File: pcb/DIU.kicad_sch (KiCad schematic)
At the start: 62 parts, among them J1 Conn_01x02_Pin, J18 Battery, J2 Conn_01x02_Pin, J3 Conn_01x03_Pin, J4 USB_OTG, J5 Conn_01x03_Socket, Q1 2N7002E, SW1 SW_SPST, SW2 SW_SPST, SW3 SW_SPST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

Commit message: Partlist refactoring
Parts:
- BZ1: Hersteller DigiKey -> (none); Nummer 668-1468-ND -> (none); Vendor (none) -> HTL; VendorId (none) -> 102851
- C1, C32: Hersteller HTL -> (none); Nummer 103250 -> (none); Vendor (none) -> HTL; VendorId (none) -> 103250
- C2: Hersteller HTL -> (none); Nummer 100139 -> (none); Vendor (none) -> HTL; VendorId (none) -> 100139
- C3: Hersteller HTL -> (none); Nummer 100140 -> (none); Vendor (none) -> HTL; VendorId (none) -> 100140
- C30, C31: Hersteller HTL -> (none); Nummer 103323 -> (none); Vendor (none) -> HTL; VendorId (none) -> 103323
- C4, C6: Hersteller HTL -> (none); Nummer 102856 -> (none); Vendor (none) -> HTL; VendorId (none) -> 102856
- C5, C7: Hersteller HTL -> (none); Nummer 100128 -> (none); Vendor (none) -> HTL; VendorId (none) -> 100128
- D89, D90: Hersteller DigiKey -> (none); Nummer 160-1830-1-ND, 160-1828-1-ND, 4 x 160-1827-1-ND -> (none); Vendor (none) -> HTL; VendorId (none) -> 103438, 103439, 4 x 103440
- D91: Hersteller HTL -> (none); Nummer 103254 -> (none); Vendor (none) -> HTL; VendorId (none) -> 103254
- F1: Hersteller DigiKey -> (none); Nummer 507-1803-1-ND -> (none); Vendor (none) -> HTL; VendorId (none) -> 101639
- H1, H2: Hersteller HTL -> (none); Nummer 101034, 101382 -> (none); Vendor (none) -> HTL; VendorId (none) -> 101034, 101382
- H3, H4: Hersteller HTL -> (none); Nummer 101017 -> (none); Vendor (none) -> HTL; VendorId (none) -> 101017
- J1, J2, J3: Hersteller HTL -> (none); Nummer 101521 -> (none); Vendor (none) -> HTL; VendorId (none) -> 101521
- J18: Hersteller DigiKey -> (none); Nummer BAT-HLD-012-SMT-ND -> (none); Vendor (none) -> HTL; VendorId (none) -> 103442
- J4: Hersteller HTL -> (none); Nummer 103441 -> (none); Vendor (none) -> HTL; VendorId (none) -> 103441
- Q1: Hersteller DigiKey -> (none); Nummer 4530-2N7002ECT-ND -> (none); Vendor (none) -> HTL; VendorId (none) -> 103443
- R100, R99: Hersteller HTL -> (none); Nummer 103202 -> (none); Vendor (none) -> HTL; VendorId (none) -> 103202
- R89, R90: Hersteller HTL -> (none); Nummer 103178 -> (none); Vendor (none) -> HTL; VendorId (none) -> 103178
- R91, R94: Hersteller HTL -> (none); Nummer 103141 -> (none); Vendor (none) -> HTL; VendorId (none) -> 103141
- R92, R93: Hersteller HTL -> (none); Nummer 103164 -> (none); Vendor (none) -> HTL; VendorId (none) -> 103164
- R95: Hersteller HTL -> (none); Nummer 103194 -> (none); Vendor (none) -> HTL
- R96: Hersteller HTL -> (none); Nummer 103202 -> (none); Vendor (none) -> HTL
- R97, R98: Hersteller HTL -> (none); Nummer 102951 -> (none); Vendor (none) -> HTL; VendorId (none) -> 102951
- SW1, SW2, SW3, SW4: Hersteller DigiKey -> (none); Nummer PTS647SM70SMTR2LFSCT-ND -> (none); Vendor (none) -> HTL; VendorId (none) -> 101614
- U1: Hersteller DigiKey -> (none); Nummer 497-3455-1-ND -> (none); Vendor (none) -> HTL; VendorId (none) -> 103444
- U15: Hersteller DigiKey -> (none); Nummer MCP7940NT-I/SNCT-ND -> (none); Vendor (none) -> HTL; VendorId (none) -> 103446
- U2: Hersteller RS -> (none); Nummer 406-580 -> (none); Vendor (none) -> HTL; VendorId (none) -> 103271
- U3: Hersteller DigiKey -> (none); Nummer ATTINY1606-SN-ND -> (none); Vendor (none) -> HTL; VendorId (none) -> 103450
- Y1: Hersteller DigiKey -> (none); Nummer 644-MU00525-32.768KCT-ND -> (none); Vendor (none) -> HTL; VendorId (none) -> 103447

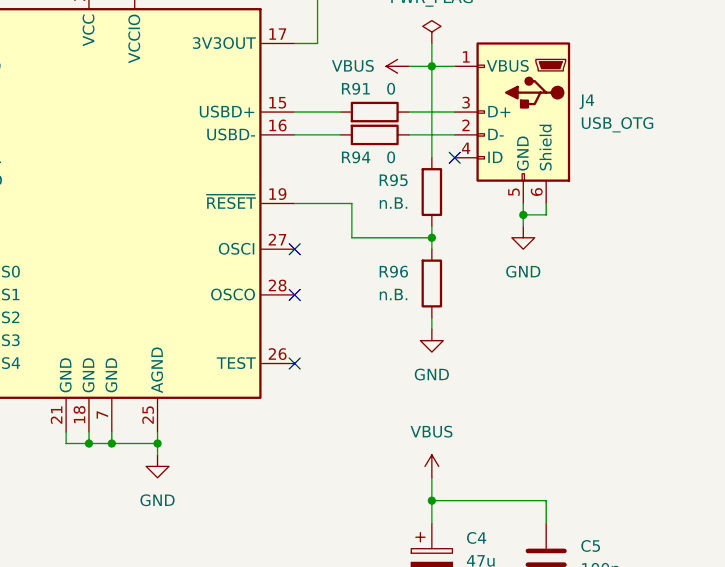
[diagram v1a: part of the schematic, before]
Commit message: Change reset circuit
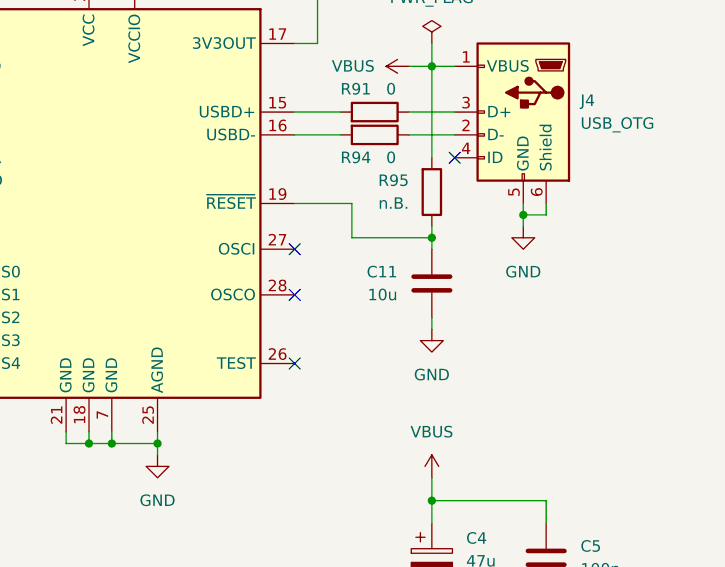
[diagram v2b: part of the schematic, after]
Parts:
- removed R96: n.B., Resistor_SMD:R_0603_1608Metric, symbol Device:R
- added C11: 10u, Capacitor_SMD:C_0603_1608Metric, symbol Device:C
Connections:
- net GND: now also C11.1
- net at R95.1, U2.19 (~{RESET}): now also C11.2
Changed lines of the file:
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@@
+    )
+  )
+  (symbol (lib_id "Device:C") (at 250.19 64.77 0) (mirror x) (unit 1)
+    (in_bom yes) (on_board yes) (dnp no) (fields_autoplaced)
+    (property "Reference" "C11" (at 246.38 63.5 0)
+      (effects (font (size 1.27 1.27)) (justify right))
+    )
+    (property "Value" "10u" (at 246.38 66.04 0)
+      (effects (font (size 1.27 1.27)) (justify right))
+    )
+    (property "Footprint" "Capacitor_SMD:C_0603_1608Metric" (at 251.1552 60.96 0)
+      (effects (font (size 1.27 1.27)) hide)
+    )
+    (property "Datasheet" "~" (at 250.19 64.77 0)
+      (effects (font (size 1.27 1.27)) hide)
+    )
+    (property "Vendor" "HTL" (at 250.19 64.77 0)
+      (effects (font (size 1.27 1.27)) hide)
+    )
+    (property "VendorId" "100137" (at 250.19 64.77 0)
+      (effects (font (size 1.27 1.27)) hide)
+    )
+    (pin "1")
+    (pin "2")
+    (instances
+      (project "DIU"
+        (path "/aa6ef36a-0508-4748-be9d-33919bd2eaaf"
+          (reference "C11") (unit 1)
+        )
+      )
     )
   )
@@
         )
       )
-    )
-  )
-  (symbol (lib_id "Device:R") (at 250.19 64.77 0) (mirror x) (unit 1)
-    (in_bom yes) (on_board yes) (dnp no) (fields_autoplaced)
-    (property "Reference" "R96" (at 247.65 63.5 0)
-      (effects (font (size 1.27 1.27)) (justify right))
-    )
-    (property "Value" "n.B." (at 247.65 66.04 0)
-      (effects (font (size 1.27 1.27)) (justify right))
-    )
-    (property "Footprint" "Resistor_SMD:R_0603_1608Metric" (at 248.412 64.77 90)
-      (effects (font (size 1.27 1.27)) hide)
-    )
-    (property "Datasheet" "~" (at 250.19 64.77 0)
-      (effects (font (size 1.27 1.27)) hide)
-    )
-    (property "Vendor" "HTL" (at 250.19 64.77 0)
-      (effects (font (size 1.27 1.27)) hide)
-    )
-    (property "VendorId" "" (at 250.19 64.77 0)
-      (effects (font (size 1.27 1.27)) hide)
-    )
-    (pin "2")
-    (pin "1")
-    (instances
-      (project "DIU"
-        (path "/aa6ef36a-0508-4748-be9d-33919bd2eaaf"
-          (reference "R96") (unit 1)
-        )
-      )

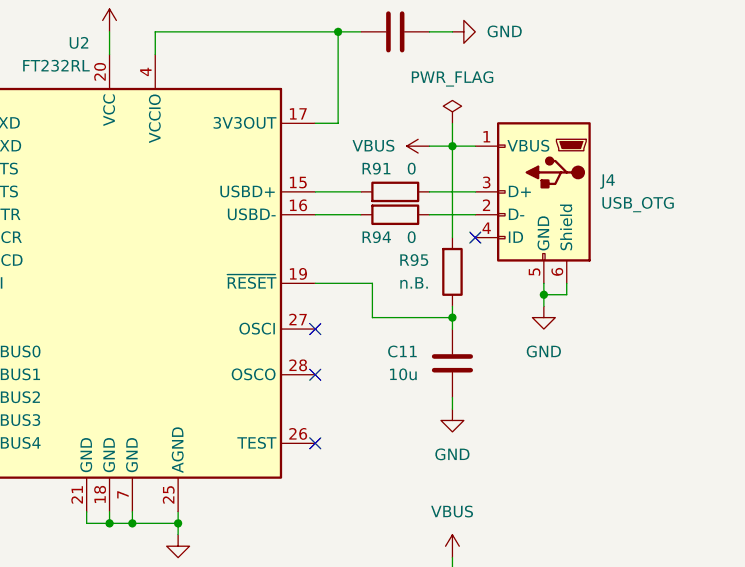
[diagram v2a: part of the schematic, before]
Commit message: Add resistor to reset circuit
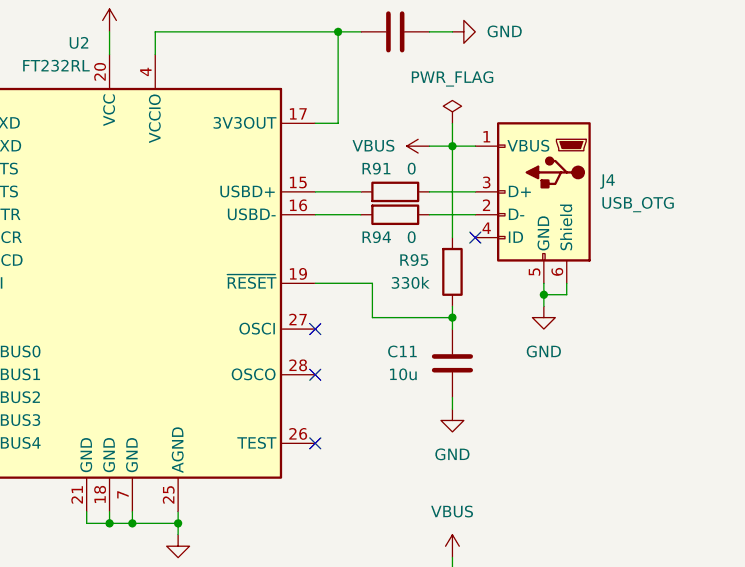
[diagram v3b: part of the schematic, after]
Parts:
- R95: value n.B. -> 330k; VendorId (none) -> 103238
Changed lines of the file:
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@@
       (effects (font (size 1.27 1.27)) (justify right))
     )
-    (property "Value" "n.B." (at 247.65 55.88 0)
+    (property "Value" "330k" (at 247.65 55.88 0)
       (effects (font (size 1.27 1.27)) (justify right))
     )
@@
       (effects (font (size 1.27 1.27)) hide)
     )
-    (property "VendorId" "" (at 250.19 54.61 0)
+    (property "VendorId" "103238" (at 250.19 54.61 0)
       (effects (font (size 1.27 1.27)) hide)
     )

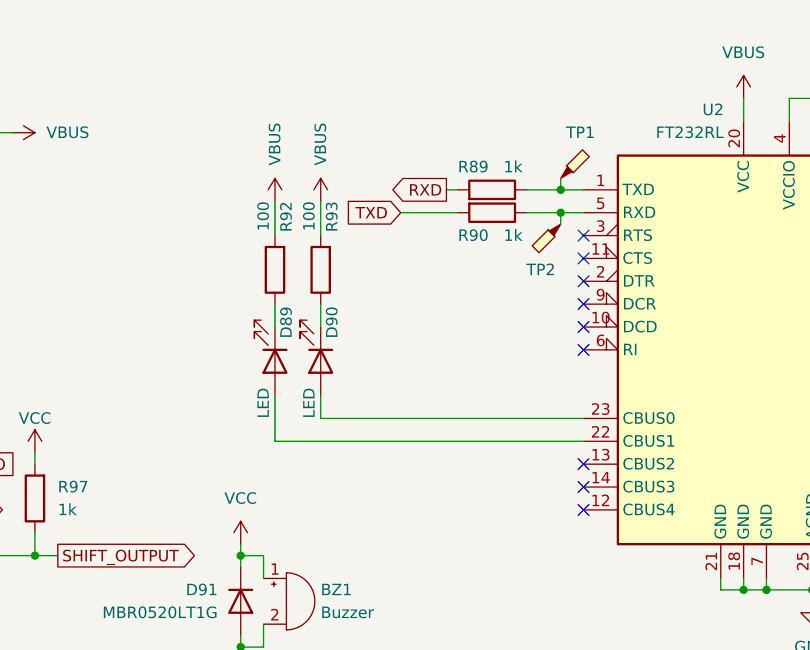
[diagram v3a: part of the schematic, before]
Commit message: Fix wrong led polarity
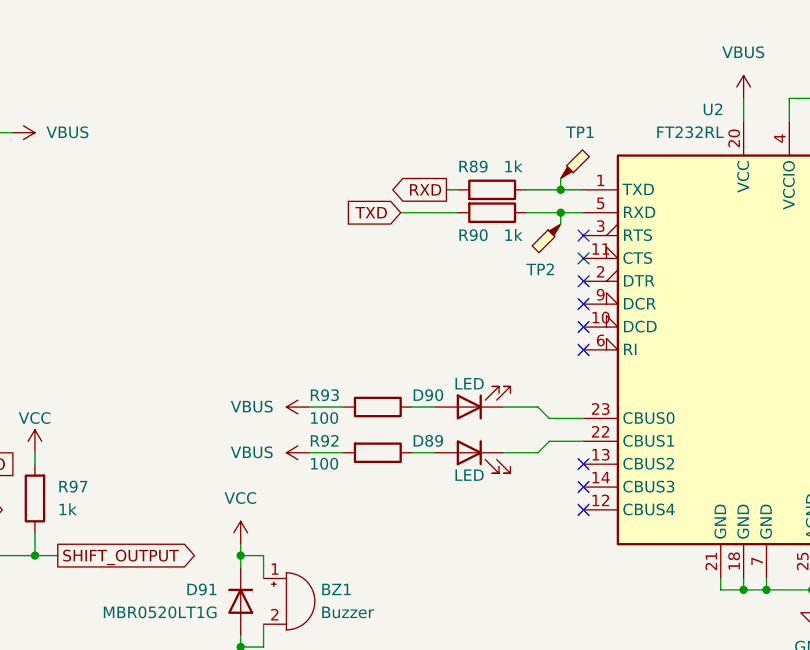
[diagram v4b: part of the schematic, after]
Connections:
- net at U2.22 (CBUS1): now also D89.1 (K); no longer D89.2 (A)
- net at U2.23 (CBUS0): now also D90.1 (K); no longer D90.2 (A)
- net at R92.1: now also D89.2 (A); no longer D89.1 (K)
- net at R93.1: now also D90.2 (A); no longer D90.1 (K)
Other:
- moved on the sheet: D89, D90, R92, R93
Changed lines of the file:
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@@
     (stroke (width 0) (type default))
   )
-  (wire (pts (xy 165.1 53.34) (xy 165.1 50.8))
+  (wire (pts (xy 177.8 62.23) (xy 175.26 62.23))
     (stroke (width 0) (type default))
   )
@@
     (stroke (width 0) (type default))
   )
-  (wire (pts (xy 165.1 43.18) (xy 165.1 39.37))
+  (wire (pts (xy 167.64 62.23) (xy 163.83 62.23))
     (stroke (width 0) (type default))
   )
@@
     (stroke (width 0) (type default))
   )
+  (wire (pts (xy 185.42 62.23) (xy 189.23 62.23))
+    (stroke (width 0) (type default))
+  )
   (wire (pts (xy 190.5 127) (xy 190.5 129.54))
     (stroke (width 0) (type default))
@@
     (stroke (width 0) (type default))
   )
+  (wire (pts (xy 190.5 66.04) (xy 194.31 66.04))
+    (stroke (width 0) (type default))
+  )
   (wire (pts (xy 76.2 40.64) (xy 76.2 43.18))
     (stroke (width 0) (type default))
@@
     (stroke (width 0) (type default))
   )
+  (wire (pts (xy 190.5 66.04) (xy 189.23 67.31))
+    (stroke (width 0) (type default))
+  )
   (wire (pts (xy 104.14 99.06) (xy 114.3 99.06))
     (stroke (width 0) (type default))
@@
     (stroke (width 0) (type default))
   )
-  (wire (pts (xy 160.02 66.04) (xy 160.02 60.96))
-    (stroke (width 0) (type default))
-  )
-  (wire (pts (xy 160.02 43.18) (xy 160.02 39.37))
+  (wire (pts (xy 167.64 67.31) (xy 163.83 67.31))
     (stroke (width 0) (type default))
   )
@@
     (stroke (width 0) (type default))
   )
-  (wire (pts (xy 72.39 30.48) (xy 76.2 30.48))
+  (wire (pts (xy 190.5 63.5) (xy 189.23 62.23))
     (stroke (width 0) (type default))
   )
-  (wire (pts (xy 194.31 66.04) (xy 160.02 66.04))
+  (wire (pts (xy 72.39 30.48) (xy 76.2 30.48))
     (stroke (width 0) (type default))
   )
@@
     (stroke (width 0) (type default))
   )
+  (wire (pts (xy 194.31 63.5) (xy 190.5 63.5))
+    (stroke (width 0) (type default))
+  )
   (wire (pts (xy 128.27 147.32) (xy 130.81 147.32))
     (stroke (width 0) (type default))
@@
     (stroke (width 0) (type default))
   )
-  (wire (pts (xy 165.1 60.96) (xy 165.1 63.5))
-    (stroke (width 0) (type default))
-  )
   (wire (pts (xy 53.34 88.9) (xy 53.34 96.52))
     (stroke (width 0) (type default))
@@
     (stroke (width 0) (type default))
   )
-  (wire (pts (xy 160.02 53.34) (xy 160.02 50.8))
+  (wire (pts (xy 177.8 67.31) (xy 175.26 67.31))
     (stroke (width 0) (type default))
   )
@@
     (stroke (width 0) (type default))
   )
-  (wire (pts (xy 194.31 63.5) (xy 165.1 63.5))
-    (stroke (width 0) (type default))
-  )
   (wire (pts (xy 250.19 58.42) (xy 250.19 59.69))
     (stroke (width 0) (type default))
@@
     (stroke (width 0) (type default))
   )
+  (wire (pts (xy 185.42 67.31) (xy 189.23 67.31))
+    (stroke (width 0) (type default))
+  )
   (wire (pts (xy 156.21 88.9) (xy 156.21 87.63))
     (stroke (width 0) (type default))
@@
     )
   )
-  (symbol (lib_id "power:VBUS") (at 160.02 39.37 0) (unit 1)
+  (symbol (lib_id "power:VBUS") (at 163.83 67.31 90) (unit 1)
     (in_bom yes) (on_board yes) (dnp no)
-    (property "Reference" "#PWR097" (at 160.02 43.18 0)
+    (property "Reference" "#PWR097" (at 167.64 67.31 0)
       (effects (font (size 1.27 1.27)) hide)
     )
-    (property "Value" "VBUS" (at 160.02 33.02 90)
+    (property "Value" "VBUS" (at 157.48 67.31 90)
       (effects (font (size 1.27 1.27)))
     )
-    (property "Footprint" "" (at 160.02 39.37 0)
+    (property "Footprint" "" (at 163.83 67.31 0)
       (effects (font (size 1.27 1.27)) hide)
     )
-    (property "Datasheet" "" (at 160.02 39.37 0)
+    (property "Datasheet" "" (at 163.83 67.31 0)
       (effects (font (size 1.27 1.27)) hide)
     )
@@
     )
   )
-  (symbol (lib_id "Device:R") (at 160.02 46.99 180) (unit 1)
+  (symbol (lib_id "Device:R") (at 171.45 67.31 270) (unit 1)
     (in_bom yes) (on_board yes) (dnp no)
-    (property "Reference" "R92" (at 161.29 39.37 90)
+    (property "Reference" "R92" (at 163.83 66.04 90)
       (effects (font (size 1.27 1.27)) (justify left))
     )
-    (property "Value" "100" (at 158.75 39.37 90)
+    (property "Value" "100" (at 163.83 68.58 90)
       (effects (font (size 1.27 1.27)) (justify left))
     )
-    (property "Footprint" "Resistor_SMD:R_0603_1608Metric" (at 161.798 46.99 90)
+    (property "Footprint" "Resistor_SMD:R_0603_1608Metric" (at 171.45 65.532 90)
       (effects (font (size 1.27 1.27)) hide)
     )
-    (property "Datasheet" "~" (at 160.02 46.99 0)
+    (property "Datasheet" "~" (at 171.45 67.31 0)
       (effects (font (size 1.27 1.27)) hide)
     )
-    (property "Vendor" "HTL" (at 160.02 46.99 0)
+    (property "Vendor" "HTL" (at 171.45 67.31 0)
       (effects (font (size 1.27 1.27)) hide)
     )
-    (property "VendorId" "103164" (at 160.02 46.99 0)
+    (property "VendorId" "103164" (at 171.45 67.31 0)
       (effects (font (size 1.27 1.27)) hide)
     )
@@
     )
   )
-  (symbol (lib_id "power:VBUS") (at 165.1 39.37 0) (unit 1)
+  (symbol (lib_id "power:VBUS") (at 163.83 62.23 90) (unit 1)
     (in_bom yes) (on_board yes) (dnp no)
-    (property "Reference" "#PWR098" (at 165.1 43.18 0)
+    (property "Reference" "#PWR098" (at 167.64 62.23 0)
       (effects (font (size 1.27 1.27)) hide)
     )
-    (property "Value" "VBUS" (at 165.1 33.02 90)
+    (property "Value" "VBUS" (at 157.48 62.23 90)
       (effects (font (size 1.27 1.27)))
     )
-    (property "Footprint" "" (at 165.1 39.37 0)
+    (property "Footprint" "" (at 163.83 62.23 0)
       (effects (font (size 1.27 1.27)) hide)
     )
-    (property "Datasheet" "" (at 165.1 39.37 0)
+    (property "Datasheet" "" (at 163.83 62.23 0)
       (effects (font (size 1.27 1.27)) hide)
     )
@@
     )
   )
-  (symbol (lib_id "Device:R") (at 165.1 46.99 180) (unit 1)
+  (symbol (lib_id "Device:R") (at 171.45 62.23 270) (unit 1)
     (in_bom yes) (on_board yes) (dnp no)
-    (property "Reference" "R93" (at 166.37 39.37 90)
+    (property "Reference" "R93" (at 163.83 60.96 90)
       (effects (font (size 1.27 1.27)) (justify left))
     )
-    (property "Value" "100" (at 163.83 39.37 90)
+    (property "Value" "100" (at 163.83 63.5 90)
       (effects (font (size 1.27 1.27)) (justify left))
     )
-    (property "Footprint" "Resistor_SMD:R_0603_1608Metric" (at 166.878 46.99 90)
+    (property "Footprint" "Resistor_SMD:R_0603_1608Metric" (at 171.45 60.452 90)
       (effects (font (size 1.27 1.27)) hide)
     )
-    (property "Datasheet" "~" (at 165.1 46.99 0)
+    (property "Datasheet" "~" (at 171.45 62.23 0)
       (effects (font (size 1.27 1.27)) hide)
     )
-    (property "Vendor" "HTL" (at 165.1 46.99 0)
+    (property "Vendor" "HTL" (at 171.45 62.23 0)
       (effects (font (size 1.27 1.27)) hide)
     )
-    (property "VendorId" "103164" (at 165.1 46.99 0)
+    (property "VendorId" "103164" (at 171.45 62.23 0)
       (effects (font (size 1.27 1.27)) hide)
     )
@@
     )
   )
-  (symbol (lib_id "Device:LED") (at 160.02 57.15 270) (unit 1)
+  (symbol (lib_id "Device:LED") (at 181.61 67.31 0) (mirror y) (unit 1)
     (in_bom yes) (on_board yes) (dnp no)
-    (property "Reference" "D89" (at 161.29 54.61 0)
+    (property "Reference" "D89" (at 175.26 66.04 0)
       (effects (font (size 1.27 1.27)) (justify right))
     )
-    (property "Value" "LED" (at 158.75 63.5 0)
-      (effects (font (size 1.27 1.27)) (justify right))
+    (property "Value" "LED" (at 181.61 69.85 0)
+      (effects (font (size 1.27 1.27)))
     )
-    (property "Footprint" "LED_SMD:LED_0603_1608Metric" (at 160.02 57.15 0)
+    (property "Footprint" "LED_SMD:LED_0603_1608Metric" (at 181.61 67.31 0)
       (effects (font (size 1.27 1.27)) hide)
     )
-    (property "Datasheet" "~" (at 160.02 57.15 0)
+    (property "Datasheet" "~" (at 181.61 67.31 0)
       (effects (font (size 1.27 1.27)) hide)
     )
-    (property "Vendor" "HTL" (at 160.02 57.15 0)
+    (property "Vendor" "HTL" (at 181.61 67.31 0)
       (effects (font (size 1.27 1.27)) hide)
     )
-    (property "VendorId" "103438, 103439, 4 x 103440" (at 160.02 57.15 0)
+    (property "VendorId" "103438, 103439, 4 x 103440" (at 181.61 67.31 0)
       (effects (font (size 1.27 1.27)) hide)
     )
@@
     )
   )
-  (symbol (lib_id "Device:LED") (at 165.1 57.15 270) (unit 1)
+  (symbol (lib_id "Device:LED") (at 181.61 62.23 180) (unit 1)
     (in_bom yes) (on_board yes) (dnp no)
-    (property "Reference" "D90" (at 166.37 54.61 0)
+    (property "Reference" "D90" (at 175.26 60.96 0)
       (effects (font (size 1.27 1.27)) (justify right))
     )
-    (property "Value" "LED" (at 163.83 63.5 0)
-      (effects (font (size 1.27 1.27)) (justify right))
+    (property "Value" "LED" (at 181.61 59.69 0)
+      (effects (font (size 1.27 1.27)))
     )
-    (property "Footprint" "LED_SMD:LED_0603_1608Metric" (at 165.1 57.15 0)
+    (property "Footprint" "LED_SMD:LED_0603_1608Metric" (at 181.61 62.23 0)
       (effects (font (size 1.27 1.27)) hide)
     )
-    (property "Datasheet" "~" (at 165.1 57.15 0)
+    (property "Datasheet" "~" (at 181.61 62.23 0)
       (effects (font (size 1.27 1.27)) hide)
     )
-    (property "Vendor" "HTL" (at 165.1 57.15 0)
+    (property "Vendor" "HTL" (at 181.61 62.23 0)
       (effects (font (size 1.27 1.27)) hide)
     )
-    (property "VendorId" "103438, 103439, 4 x 103440" (at 165.1 57.15 0)
+    (property "VendorId" "103438, 103439, 4 x 103440" (at 181.61 62.23 0)
       (effects (font (size 1.27 1.27)) hide)
     )

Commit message: Adapt vendor-ids on leds
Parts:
- D89, D90: VendorId 103438, 103439, 4 x 103440 -> 103440
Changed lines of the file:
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@@
       (effects (font (size 1.27 1.27)) hide)
     )
-    (property "VendorId" "103438, 103439, 4 x 103440" (at 181.61 67.31 0)
+    (property "VendorId" "103440" (at 181.61 67.31 0)
       (effects (font (size 1.27 1.27)) hide)
     )
@@
       (effects (font (size 1.27 1.27)) hide)
     )
-    (property "VendorId" "103438, 103439, 4 x 103440" (at 181.61 62.23 0)
-      (effects (font (size 1.27 1.27)) hide)
-    )
+    (property "VendorId" "103440" (at 181.61 62.23 0)
+      (effects (font (size 1.27 1.27)) hide)
+    )
